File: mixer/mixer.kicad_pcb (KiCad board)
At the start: 2 copper layers, 35.6 x 38.1 mm, 20 parts, among them J1 in0, J2 in1, J3 in2, J4 out, J5 Conn_01x02, U1 OPA2134, U2 TLE2426xD

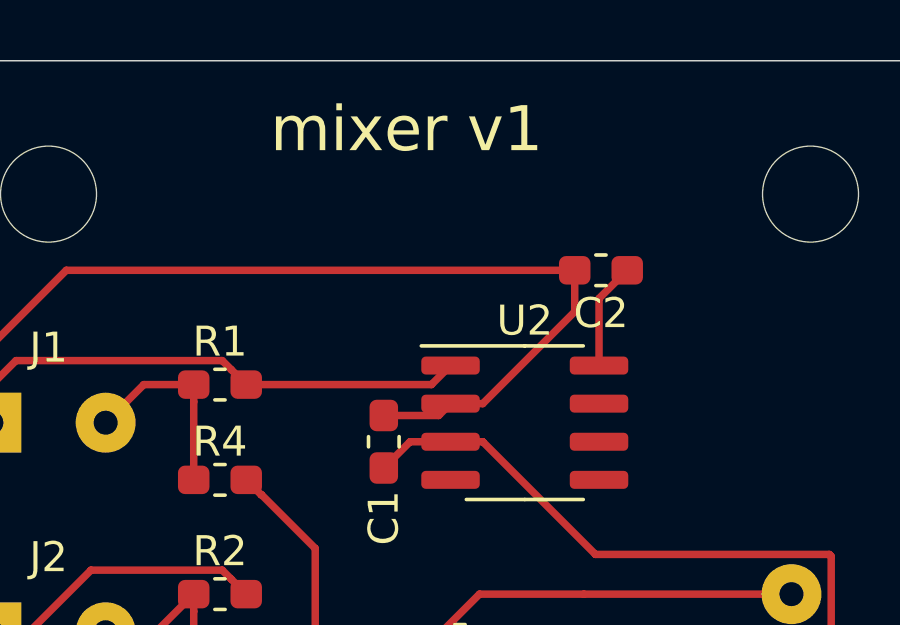
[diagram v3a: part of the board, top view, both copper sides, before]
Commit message: Dual bypass capacitors
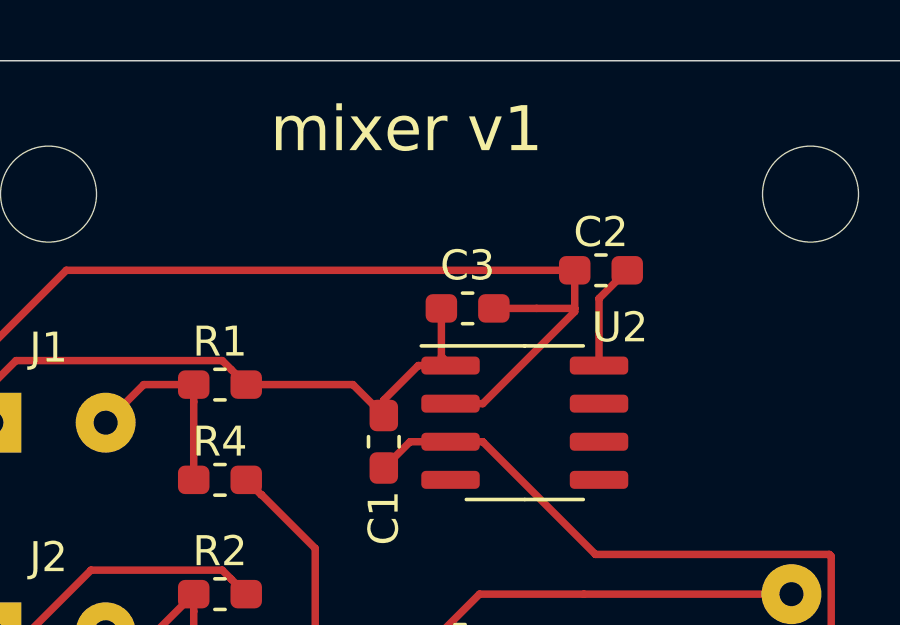
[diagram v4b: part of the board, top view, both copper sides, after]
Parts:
- added C3: 1u, Capacitor_SMD:C_0603_1608Metric_Pad1.05x0.95mm_HandSolder, F.Cu at (151.1, 69.2)
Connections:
- C1 pad 1: GND -> GNDA
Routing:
- net GNDA: track 84.9 -> 88.1 mm
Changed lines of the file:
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@@
     (thickness 1.6)
     (drawings 5)
-    (tracks 89)
+    (tracks 95)
     (zones 0)
-    (modules 20)
+    (modules 21)
     (nets 10)
   )
@@
       (outputformat 1)
       (mirror false)
-      (drillshape 1)
+      (drillshape 0)
       (scaleselection 1)
-      (outputdirectory ""))
+      (outputdirectory "gerber/"))
   )
   (net 0 "")
@@
       (effects (font (size 1 1) (thickness 0.15)))
     )
-    (fp_text value 1u (at -2.54 0 90) (layer F.Fab)
+    (fp_text value 1u (at -2.54 0 90) (layer F.Fab) hide
       (effects (font (size 1 1) (thickness 0.15)))
     )
@@
       (net 1 +9V))
     (pad 1 smd roundrect (at -0.875 0 270) (size 1.05 0.95) (layers F.Cu F.Paste F.Mask) (roundrect_rratio 0.25)
-      (net 2 GND))
+      (net 4 GNDA))
     (model ${KISYS3DMOD}/Capacitor_SMD.3dshapes/C_0603_1608Metric.wrl
       (at (xyz 0 0 0))
@@
     (tags "capacitor handsolder")
     (attr smd)
-    (fp_text reference C2 (at 0 -1.43) (layer F.SilkS)
-      (effects (font (size 1 1) (thickness 0.15)))
-    )
-    (fp_text value 1u (at 0 1.43) (layer F.Fab)
+    (fp_text reference C2 (at 0 1.27) (layer F.SilkS)
+      (effects (font (size 1 1) (thickness 0.15)))
+    )
+    (fp_text value 1u (at 0 1.43) (layer F.Fab) hide
       (effects (font (size 1 1) (thickness 0.15)))
     )
@@
     (tags "SOIC SO")
     (attr smd)
-    (fp_text reference U2 (at 0 -3.4) (layer F.SilkS)
+    (fp_text reference U2 (at 3.175 -3.175) (layer F.SilkS)
       (effects (font (size 1 1) (thickness 0.15)))
     )
@@
     )
   )
+  (module Capacitor_SMD:C_0603_1608Metric_Pad1.05x0.95mm_HandSolder (layer F.Cu)
+    (at 151.13 69.215)
+    (descr "Capacitor SMD 0603 (1608 Metric), square (rectangular) end terminal, IPC_7351 nominal with elongated pad for handsoldering. (Body size source: http://www.tortai-tech.com/upload/download/2011102023233369053.pdf), generated with kicad-footprint-generator")
+    (tags "capacitor handsolder")
+    (attr smd)
+    (fp_text reference C3 (at 0 -1.43) (layer F.SilkS)
+      (effects (font (size 1 1) (thickness 0.15)))
+    )
+    (fp_text value 1u (at 0 1.43) (layer F.Fab) hide
+      (effects (font (size 1 1) (thickness 0.15)))
+    )
+    (fp_line (start -0.8 0.4) (end -0.8 -0.4) (layer F.Fab) (width 0.1))
+    (fp_line (start -0.8 -0.4) (end 0.8 -0.4) (layer F.Fab) (width 0.1))
+    (fp_line (start 0.8 -0.4) (end 0.8 0.4) (layer F.Fab) (width 0.1))
+    (fp_line (start 0.8 0.4) (end -0.8 0.4) (layer F.Fab) (width 0.1))
+    (fp_line (start -0.171267 -0.51) (end 0.171267 -0.51) (layer F.SilkS) (width 0.12))
+    (fp_line (start -0.171267 0.51) (end 0.171267 0.51) (layer F.SilkS) (width 0.12))
+    (fp_line (start -1.65 0.73) (end -1.65 -0.73) (layer F.CrtYd) (width 0.05))
+    (fp_line (start -1.65 -0.73) (end 1.65 -0.73) (layer F.CrtYd) (width 0.05))
+    (fp_line (start 1.65 -0.73) (end 1.65 0.73) (layer F.CrtYd) (width 0.05))
+    (fp_line (start 1.65 0.73) (end -1.65 0.73) (layer F.CrtYd) (width 0.05))
+    (fp_text user %R (at 0 0) (layer F.Fab)
+      (effects (font (size 0.4 0.4) (thickness 0.06)))
+    )
+    (pad 1 smd roundrect (at -0.875 0) (size 1.05 0.95) (layers F.Cu F.Paste F.Mask) (roundrect_rratio 0.25)
+      (net 4 GNDA))
+    (pad 2 smd roundrect (at 0.875 0) (size 1.05 0.95) (layers F.Cu F.Paste F.Mask) (roundrect_rratio 0.25)
+      (net 2 GND))
+    (model ${KISYS3DMOD}/Capacitor_SMD.3dshapes/C_0603_1608Metric.wrl
+      (at (xyz 0 0 0))
+      (scale (xyz 1 1 1))
+      (rotate (xyz 0 0 0))
+    )
+  )
   (gr_text "mixer v1" (at 149.098 63.246) (layer F.SilkS)
     (effects (font (size 1.5 1.5) (thickness 0.3)))
@@
   (segment (start 154.7 69.325) (end 151.635 72.39) (width 0.25) (layer F.Cu) (net 2))
   (segment (start 151.635 72.39) (end 150.56 72.39) (width 0.25) (layer F.Cu) (net 2))
-  (segment (start 154.7 67.945) (end 154.7 69.325) (width 0.25) (layer F.Cu) (net 2))
-  (segment (start 150.165 72.785) (end 150.56 72.39) (width 0.25) (layer F.Cu) (net 2))
-  (segment (start 148.336 72.785) (end 150.165 72.785) (width 0.25) (layer F.Cu) (net 2))
   (segment (start 150.56 94.55) (end 147.955 97.155) (width 0.25) (layer F.Cu) (net 2))
   (segment (start 150.56 86.995) (end 150.56 94.55) (width 0.25) (layer F.Cu) (net 2))
@@
   (segment (start 133.35 87.673982) (end 142.831018 97.155) (width 0.25) (layer F.Cu) (net 2))
   (segment (start 133.35 72.346018) (end 133.35 87.673982) (width 0.25) (layer F.Cu) (net 2))
+  (segment (start 153.43 69.215) (end 154.7 69.215) (width 0.25) (layer F.Cu) (net 2))
+  (segment (start 152.005 69.215) (end 153.43 69.215) (width 0.25) (layer F.Cu) (net 2))
+  (segment (start 154.7 69.215) (end 154.7 69.325) (width 0.25) (layer F.Cu) (net 2))
+  (segment (start 154.7 67.945) (end 154.7 69.215) (width 0.25) (layer F.Cu) (net 2))
   (segment (start 155.51 68.885) (end 156.45 67.945) (width 0.25) (layer F.Cu) (net 3))
   (segment (start 155.51 71.12) (end 155.51 68.885) (width 0.25) (layer F.Cu) (net 3))
@@
   (segment (start 135.255 85.74551) (end 136.07552 84.92499) (width 0.25) (layer F.Cu) (net 4))
   (segment (start 135.255 86.995) (end 135.255 85.74551) (width 0.25) (layer F.Cu) (net 4))
-  (segment (start 149.925 71.755) (end 150.56 71.12) (width 0.25) (layer F.Cu) (net 4))
-  (segment (start 143.75 71.755) (end 149.925 71.755) (width 0.25) (layer F.Cu) (net 4))
   (segment (start 158.75 85.725) (end 161.925 82.55) (width 0.25) (layer F.Cu) (net 4))
   (segment (start 155.51 85.725) (end 158.75 85.725) (width 0.25) (layer F.Cu) (net 4))
@@
   (segment (start 144.786 90.424) (end 149.485 85.725) (width 0.25) (layer F.Cu) (net 4))
   (segment (start 137.43451 90.424) (end 144.786 90.424) (width 0.25) (layer F.Cu) (net 4))
+  (segment (start 150.255 70.815) (end 150.56 71.12) (width 0.25) (layer F.Cu) (net 4))
+  (segment (start 150.255 69.215) (end 150.255 70.815) (width 0.25) (layer F.Cu) (net 4))
+  (segment (start 147.306 71.755) (end 148.336 72.785) (width 0.25) (layer F.Cu) (net 4))
+  (segment (start 143.75 71.755) (end 147.306 71.755) (width 0.25) (layer F.Cu) (net 4))
+  (segment (start 148.336 72.269) (end 148.336 72.785) (width 0.25) (layer F.Cu) (net 4))
+  (segment (start 149.485 71.12) (end 148.336 72.269) (width 0.25) (layer F.Cu) (net 4))
+  (segment (start 150.56 71.12) (end 149.485 71.12) (width 0.25) (layer F.Cu) (net 4))
   (segment (start 140.335 71.755) (end 142 71.755) (width 0.25) (layer F.Cu) (net 5))
   (segment (start 139.065 73.025) (end 140.335 71.755) (width 0.25) (layer F.Cu) (net 5))

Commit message: Silkscreen
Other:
- board text added: "+9v"
- board text added: "-"
- board text added: "gnd"
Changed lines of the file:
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@@
   (general
     (thickness 1.6)
-    (drawings 5)
+    (drawings 9)
     (tracks 95)
     (zones 0)
@@
     (tags connector)
     (attr virtual)
-    (fp_text reference J5 (at -3.175 0.635) (layer F.SilkS)
+    (fp_text reference J5 (at -3.175 0.635) (layer F.SilkS) hide
       (effects (font (size 1 1) (thickness 0.15)))
     )
@@
       (rotate (xyz 0 0 0))
     )
+  )
+  (gr_text gnd (at 133.985 83.185 90) (layer F.SilkS)
+    (effects (font (size 1.5 1.5) (thickness 0.3)))
+  )
+  (gr_text gnd (at 165.1 82.55 90) (layer F.SilkS)
+    (effects (font (size 1.5 1.5) (thickness 0.3)))
+  )
+  (gr_text - (at 144.78 97.155) (layer F.SilkS)
+    (effects (font (size 1.5 1.5) (thickness 0.3)))
+  )
+  (gr_text +9v (at 155.575 97.155) (layer F.SilkS)
+    (effects (font (size 1.5 1.5) (thickness 0.3)))
   )
   (gr_text "mixer v1" (at 149.098 63.246) (layer F.SilkS)
@@
   (segment (start 142 86.3) (end 142 88.9) (width 0.25) (layer F.Cu) (net 7))
   (segment (start 142 85.725) (end 142 86.3) (width 0.25) (layer F.Cu) (net 7))
-  (segment (start 150.754072 82.990928) (end 150.56 83.185) (width 0.25) (layer F.Cu) (net 9))
-  (segment (start 155.005 78.74) (end 161.925 78.74) (width 0.25) (layer F.Cu) (net 9))
-  (segment (start 150.56 80.823) (end 150.001 80.264) (width 0.25) (layer F.Cu) (net 9))
-  (segment (start 150.56 83.185) (end 150.56 80.823) (width 0.25) (layer F.Cu) (net 9))
-  (segment (start 151.525 78.74) (end 155.005 78.74) (width 0.25) (layer F.Cu) (net 9))
-  (segment (start 150.001 80.264) (end 151.525 78.74) (width 0.25) (layer F.Cu) (net 9))
   (segment (start 144.263072 75.429072) (end 146.05 77.216) (width 0.25) (layer F.Cu) (net 8))
   (segment (start 146.05 86.6) (end 143.75 88.9) (width 0.25) (layer F.Cu) (net 8))
@@
   (segment (start 151.86001 84.22999) (end 151.635 84.455) (width 0.25) (layer F.Cu) (net 8))
   (segment (start 151.751 80.264) (end 151.751 80.839) (width 0.25) (layer F.Cu) (net 8))
+  (segment (start 150.754072 82.990928) (end 150.56 83.185) (width 0.25) (layer F.Cu) (net 9))
+  (segment (start 155.005 78.74) (end 161.925 78.74) (width 0.25) (layer F.Cu) (net 9))
+  (segment (start 150.56 80.823) (end 150.001 80.264) (width 0.25) (layer F.Cu) (net 9))
+  (segment (start 150.56 83.185) (end 150.56 80.823) (width 0.25) (layer F.Cu) (net 9))
+  (segment (start 151.525 78.74) (end 155.005 78.74) (width 0.25) (layer F.Cu) (net 9))
+  (segment (start 150.001 80.264) (end 151.525 78.74) (width 0.25) (layer F.Cu) (net 9))
 )
